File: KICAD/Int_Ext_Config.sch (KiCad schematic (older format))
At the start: 7 parts, among them J3 Conn_01x17_Male

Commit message: removed legacy symbols
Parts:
- removed J3: Conn_01x17_Male, symbol Connector:Conn_01x17_Male
- removed JP1: CC-CV, symbol sesame-fonctionnel-rescue:Jumper-device
- removed JP2, JP3: Jumper, symbol sesame-fonctionnel-rescue:Jumper-device
- removed R5, R6, R7: R, symbol sesame-fonctionnel-rescue:R-device
- added J?: Conn_01x17_Male, symbol Connector:Conn_01x17_Male
- added JP? (x3): Jumper, symbol Device:Jumper
- added R? (x3): R, symbol Device:R
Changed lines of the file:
@@
 $Descr A4 11693 8268
 encoding utf-8
-Sheet 10 15
+Sheet 9 15
 Title ""
 Date ""
@@
 Text GLabel 5300 5450 2    50   Output ~ 0
 Ex_CC_CV_Mode
-Text GLabel 5750 3200 2    50   Output ~ 0
+Text GLabel 6100 3200 2    50   Output ~ 0
 Mode
-$Comp
-L sesame-fonctionnel-rescue:Jumper-device JP3
-U 1 1 6188609D
-P 5000 3200
-AR Path="/6188609D" Ref="JP3"  Part="1"
-AR Path="/618748E2/6188609D" Ref="JP3"  Part="1"
-F 0 "JP3" H 5000 3464 50  0000 C CNN
-F 1 "Jumper" H 5000 3373 50  0000 C CNN
-F 2 "" H 5000 3200 50  0001 C CNN
-F 3 "~" H 5000 3200 50  0001 C CNN
-	1    5000 3200
-	1    0    0    -1
-$EndComp
 Wire Wire Line
 	4700 3200 4650 3200
@@
 Wire Wire Line
 	5650 3950 5650 4150
-Wire Wire Line
-	5650 4150 5000 4150
-Wire Wire Line
-	5450 4050 5000 4050
 Wire Wire Line
 	5450 3950 5450 4050
@@
 Wire Wire Line
 	5300 4950 5000 4950
-Wire Wire Line
-	5300 4250 5000 4250
-Wire Wire Line
-	5000 4350 5300 4350
-Wire Wire Line
-	5300 4450 5000 4450
-Wire Wire Line
-	5000 4550 5300 4550
-Connection ~ 5650 3200
-Wire Wire Line
-	5650 3200 5750 3200
-Wire Wire Line
-	5300 3200 5650 3200
 Connection ~ 4650 3200
 Wire Wire Line
-	5500 1900 5500 1800
-Connection ~ 5500 1900
-Wire Wire Line
-	5650 1900 5500 1900
-Wire Wire Line
-	5650 2300 5650 3200
-Connection ~ 5500 2800
-Wire Wire Line
-	5500 2800 5750 2800
-Connection ~ 5350 2400
-Wire Wire Line
-	5750 2400 5350 2400
-Wire Wire Line
-	5500 2300 5500 2800
+	5600 1900 5600 1800
 Connection ~ 4650 2800
 Wire Wire Line
@@
 Wire Wire Line
 	4700 2800 4650 2800
-$Comp
-L sesame-fonctionnel-rescue:Jumper-device JP1
-U 1 1 618860D7
-P 5000 2400
-AR Path="/618860D7" Ref="JP1"  Part="1"
-AR Path="/618748E2/618860D7" Ref="JP1"  Part="1"
-F 0 "JP1" H 5000 2664 50  0000 C CNN
-F 1 "CC-CV" H 5000 2573 50  0000 C CNN
-F 2 "" H 5000 2400 50  0001 C CNN
-F 3 "~" H 5000 2400 50  0001 C CNN
-	1    5000 2400
-	1    0    0    -1
-$EndComp
-$Comp
-L sesame-fonctionnel-rescue:Jumper-device JP2
-U 1 1 618860DD
-P 5000 2800
-AR Path="/618860DD" Ref="JP2"  Part="1"
-AR Path="/618748E2/618860DD" Ref="JP2"  Part="1"
-F 0 "JP2" H 5000 3064 50  0000 C CNN
-F 1 "Jumper" H 5000 2973 50  0000 C CNN
-F 2 "" H 5000 2800 50  0001 C CNN
-F 3 "~" H 5000 2800 50  0001 C CNN
-	1    5000 2800
-	1    0    0    -1
-$EndComp
-Text GLabel 5750 2400 2    50   Output ~ 0
+Text GLabel 6100 2400 2    50   Output ~ 0
 CC_CV_Mode
-$Comp
-L sesame-fonctionnel-rescue:R-device R5
-U 1 1 618860E4
-P 5350 2150
-AR Path="/618860E4" Ref="R5"  Part="1"
-AR Path="/618748E2/618860E4" Ref="R5"  Part="1"
-F 0 "R5" H 5250 2300 50  0000 L CNN
-F 1 "R" H 5250 2200 50  0000 L CNN
-F 2 "" V 5280 2150 50  0001 C CNN
-F 3 "~" H 5350 2150 50  0001 C CNN
-	1    5350 2150
-	1    0    0    -1
-$EndComp
 $Comp
 L power:VCC #PWR0112
 U 1 1 618860EA
-P 5500 1800
-F 0 "#PWR0112" H 5500 1650 50  0001 C CNN
-F 1 "VCC" H 5515 1973 50  0000 C CNN
-F 2 "" H 5500 1800 50  0001 C CNN
-F 3 "" H 5500 1800 50  0001 C CNN
-	1    5500 1800
+P 5600 1800
+F 0 "#PWR0112" H 5600 1650 50  0001 C CNN
+F 1 "VCC" H 5615 1973 50  0000 C CNN
+F 2 "" H 5600 1800 50  0001 C CNN
+F 3 "" H 5600 1800 50  0001 C CNN
+	1    5600 1800
 	1    0    0    -1
 $EndComp
 Wire Wire Line
 	5350 2400 5300 2400
-Wire Wire Line
-	5350 2300 5350 2400
-Text GLabel 5750 2800 2    50   Output ~ 0
+Text GLabel 6100 2800 2    50   Output ~ 0
 Dir
-$Comp
-L sesame-fonctionnel-rescue:R-device R6
-U 1 1 618860F3
-P 5500 2150
-AR Path="/618860F3" Ref="R6"  Part="1"
-AR Path="/618748E2/618860F3" Ref="R6"  Part="1"
-F 0 "R6" H 5400 2300 50  0000 L CNN
-F 1 "R" H 5400 2200 50  0000 L CNN
-F 2 "" V 5430 2150 50  0001 C CNN
-F 3 "~" H 5500 2150 50  0001 C CNN
-	1    5500 2150
-	1    0    0    -1
-$EndComp
-Wire Wire Line
-	5500 2800 5300 2800
-Wire Wire Line
-	5500 2000 5500 1900
-Wire Wire Line
-	5500 1900 5350 1900
 Wire Wire Line
 	5350 1900 5350 2000
-$Comp
-L sesame-fonctionnel-rescue:R-device R7
-U 1 1 618860FD
-P 5650 2150
-AR Path="/618860FD" Ref="R7"  Part="1"
-AR Path="/618748E2/618860FD" Ref="R7"  Part="1"
-F 0 "R7" H 5550 2300 50  0000 L CNN
-F 1 "R" H 5550 2200 50  0000 L CNN
-F 2 "" V 5580 2150 50  0001 C CNN
-F 3 "~" H 5650 2150 50  0001 C CNN
-	1    5650 2150
-	1    0    0    -1
-$EndComp
-Wire Wire Line
-	5650 2000 5650 1900
 Text GLabel 5300 4750 2    50   Output ~ 0
 Ex_PWM
@@
 Text GLabel 5300 4650 2    50   Output ~ 0
 Ex_Consign
-$Comp
-L Connector:Conn_01x17_Male J3
-U 1 1 61886109
-P 4800 4750
-F 0 "J3" H 4908 5731 50  0000 C CNN
-F 1 "Conn_01x17_Male" H 4908 5640 50  0000 C CNN
-F 2 "" H 4800 4750 50  0001 C CNN
-F 3 "~" H 4800 4750 50  0001 C CNN
-	1    4800 4750
-	1    0    0    -1
-$EndComp
-Wire Wire Line
-	5300 4650 5000 4650
 Text HLabel 5300 4250 2    50   Input ~ 0
 Current_Sens_L
@@
 Text HLabel 5300 4550 2    50   Input ~ 0
 Voltage_Sens_R
+$Comp
+L Device:Jumper JP?
+U 1 1 61093A28
+P 5000 2800
+F 0 "JP?" H 5000 3064 50  0000 C CNN
+F 1 "Jumper" H 5000 2973 50  0000 C CNN
+F 2 "" H 5000 2800 50  0001 C CNN
+F 3 "~" H 5000 2800 50  0001 C CNN
+	1    5000 2800
+	1    0    0    -1
+$EndComp
+$Comp
+L Device:Jumper JP?
+U 1 1 61098F8F
+P 5000 2400
+F 0 "JP?" H 5000 2664 50  0000 C CNN
+F 1 "Jumper" H 5000 2573 50  0000 C CNN
+F 2 "" H 5000 2400 50  0001 C CNN
+F 3 "~" H 5000 2400 50  0001 C CNN
+	1    5000 2400
+	1    0    0    -1
+$EndComp
+$Comp
+L Device:Jumper JP?
+U 1 1 6109AD40
+P 5000 3200
+F 0 "JP?" H 5000 3464 50  0000 C CNN
+F 1 "Jumper" H 5000 3373 50  0000 C CNN
+F 2 "" H 5000 3200 50  0001 C CNN
+F 3 "~" H 5000 3200 50  0001 C CNN
+	1    5000 3200
+	1    0    0    -1
+$EndComp
+$Comp
+L Device:R R?
+U 1 1 6109B89A
+P 5350 2150
+F 0 "R?" H 5420 2196 50  0000 L CNN
+F 1 "R" H 5420 2105 50  0000 L CNN
+F 2 "" V 5280 2150 50  0001 C CNN
+F 3 "~" H 5350 2150 50  0001 C CNN
+	1    5350 2150
+	1    0    0    -1
+$EndComp
+$Comp
+L Device:R R?
+U 1 1 6109EABF
+P 5600 2150
+F 0 "R?" H 5670 2196 50  0000 L CNN
+F 1 "R" H 5670 2105 50  0000 L CNN
+F 2 "" V 5530 2150 50  0001 C CNN
+F 3 "~" H 5600 2150 50  0001 C CNN
+	1    5600 2150
+	1    0    0    -1
+$EndComp
+$Comp
+L Device:R R?
+U 1 1 6109F746
+P 5850 2150
+F 0 "R?" H 5920 2196 50  0000 L CNN
+F 1 "R" H 5920 2105 50  0000 L CNN
+F 2 "" V 5780 2150 50  0001 C CNN
+F 3 "~" H 5850 2150 50  0001 C CNN
+	1    5850 2150
+	1    0    0    -1
+$EndComp
+Connection ~ 5600 1900
+Wire Wire Line
+	5350 1900 5600 1900
+Wire Wire Line
+	5600 2000 5600 1900
+Wire Wire Line
+	5850 1900 5850 2000
+Wire Wire Line
+	5600 1900 5850 1900
+Wire Wire Line
+	5300 3200 5850 3200
+Wire Wire Line
+	5300 2800 5600 2800
+Wire Wire Line
+	5350 2300 5350 2400
+Connection ~ 5600 2800
+Wire Wire Line
+	5600 2800 6100 2800
+Wire Wire Line
+	5600 2300 5600 2800
+Wire Wire Line
+	5850 2300 5850 3200
+Connection ~ 5850 3200
+Wire Wire Line
+	5850 3200 6100 3200
+Wire Wire Line
+	5350 2400 6100 2400
+Connection ~ 5350 2400
+$Comp
+L Connector:Conn_01x17_Male J?
+U 1 1 610AA20B
+P 4800 4750
+F 0 "J?" H 4908 5731 50  0000 C CNN
+F 1 "Conn_01x17_Male" H 4908 5640 50  0000 C CNN
+F 2 "" H 4800 4750 50  0001 C CNN
+F 3 "~" H 4800 4750 50  0001 C CNN
+	1    4800 4750
+	1    0    0    -1
+$EndComp
+Wire Wire Line
+	5000 4650 5300 4650
+Wire Wire Line
+	5300 4550 5000 4550
+Wire Wire Line
+	5000 4450 5300 4450
+Wire Wire Line
+	5300 4350 5000 4350
+Wire Wire Line
+	5000 4250 5300 4250
+Wire Wire Line
+	5650 4150 5000 4150
+Wire Wire Line
+	5000 4050 5450 4050
 $EndSCHEMATC

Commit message: a ton of new stuff. V0.8
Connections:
- net labels added: +6V, +7V
- net labels removed: +2V5, VCC
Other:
- note added: "A voir au dernier moment"
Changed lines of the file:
@@
 $Descr A4 11693 8268
 encoding utf-8
-Sheet 8 15
+Sheet 8 16
 Title ""
 Date ""
@@
 Wire Wire Line
 	5450 3950 5450 4050
-$Comp
-L power:VCC #PWR0110
-U 1 1 618860AB
-P 5450 3950
-F 0 "#PWR0110" H 5450 3800 50  0001 C CNN
-F 1 "VCC" H 5465 4123 50  0000 C CNN
-F 2 "" H 5450 3950 50  0001 C CNN
-F 3 "" H 5450 3950 50  0001 C CNN
-	1    5450 3950
-	1    0    0    -1
-$EndComp
-$Comp
-L power:+2V5 #PWR0111
-U 1 1 618860B1
-P 5650 3950
-F 0 "#PWR0111" H 5650 3800 50  0001 C CNN
-F 1 "+2V5" H 5665 4123 50  0000 C CNN
-F 2 "" H 5650 3950 50  0001 C CNN
-F 3 "" H 5650 3950 50  0001 C CNN
-	1    5650 3950
-	1    0    0    -1
-$EndComp
 Text GLabel 5300 5150 2    50   Output ~ 0
 Ex_Rearm
@@
 Text GLabel 6100 2400 2    50   Output ~ 0
 CC_CV_Mode
-$Comp
-L power:VCC #PWR0112
-U 1 1 618860EA
-P 5600 1800
-F 0 "#PWR0112" H 5600 1650 50  0001 C CNN
-F 1 "VCC" H 5615 1973 50  0000 C CNN
-F 2 "" H 5600 1800 50  0001 C CNN
-F 3 "" H 5600 1800 50  0001 C CNN
-	1    5600 1800
-	1    0    0    -1
-$EndComp
 Wire Wire Line
 	5350 2400 5300 2400
@@
 Wire Wire Line
 	5000 4050 5450 4050
+Text Notes 4550 950  0    100  ~ 20
+A voir au dernier moment
+$Comp
+L Sesame:+7V #PWR0128
+U 1 1 61485513
+P 5600 1800
+F 0 "#PWR0128" H 5600 1650 50  0001 C CNN
+F 1 "+7V" H 5615 1973 50  0000 C CNN
+F 2 "" H 5600 1800 50  0001 C CNN
+F 3 "" H 5600 1800 50  0001 C CNN
+	1    5600 1800
+	1    0    0    -1
+$EndComp
+$Comp
+L Sesame:+7V #PWR0129
+U 1 1 61487244
+P 5450 3950
+F 0 "#PWR0129" H 5450 3800 50  0001 C CNN
+F 1 "+7V" H 5465 4123 50  0000 C CNN
+F 2 "" H 5450 3950 50  0001 C CNN
+F 3 "" H 5450 3950 50  0001 C CNN
+	1    5450 3950
+	1    0    0    -1
+$EndComp
+$Comp
+L power:+6V #PWR0130
+U 1 1 61487948
+P 5650 3950
+F 0 "#PWR0130" H 5650 3800 50  0001 C CNN
+F 1 "+6V" H 5665 4123 50  0000 C CNN
+F 2 "" H 5650 3950 50  0001 C CNN
+F 3 "" H 5650 3950 50  0001 C CNN
+	1    5650 3950
+	1    0    0    -1
+$EndComp
 $EndSCHEMATC

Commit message: minor cleanup
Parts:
- removed J?: Conn_01x17_Male, symbol Connector:Conn_01x17_Male
- removed JP? (x3): Jumper, symbol Device:Jumper
- removed R? (x3): R, symbol Device:R
- added J?: Conn_02x16_Odd_Even, symbol Connector_Generic:Conn_02x16_Odd_Even
- added JP? (x5): Jumper_NC_Dual, symbol Device:Jumper_NC_Dual
- added R? (x3): R, symbol Device:R
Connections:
- net CC_CV_Mode: now also J?.32 (Pin_32), R?.2
- net Current_Sens_L: now also J?.8 (Pin_8)
- net Current_Sens_R: now also J?.12 (Pin_12)
- net Dir: now also J?.30 (Pin_30), R?.2
- net GND: now also J?.1 (Pin_1), J?.11 (Pin_11), J?.13 (Pin_13), J?.15 (Pin_15), J?.17 (Pin_17), J?.19 (Pin_19), J?.21 (Pin_21), J?.23 (Pin_23), J?.25 (Pin_25), J?.27 (Pin_27), J?.29 (Pin_29), J?.3 (Pin_3), J?.31 (Pin_31), J?.5 (Pin_5), J?.7 (Pin_7), J?.9 (Pin_9), JP?.1, JP?.1, JP?.1
- net Mode: now also J?.28 (Pin_28), R?.2
- net Voltage_Sens_L: now also J?.10 (Pin_10)
- net Voltage_Sens_R: now also J?.14 (Pin_14)
- new net: JP?.2, R?.1 (x3)
- new net Ext_Current_Tresh: J?.22 (Pin_22)
- new net Ext_PWM: J?.18 (Pin_18), JP?.3
- new net Ext_Rearm: J?.26 (Pin_26)
- new net Ext_Setpoint: J?.16 (Pin_16)
- new net Ext_Voltage_Tresh: J?.24 (Pin_24)
- new net INT_PWM: JP?.1
- new net PWM: JP?.2
- new net VCC: J?.2 (Pin_2), J?.4 (Pin_4), JP?.3, JP?.3, JP?.3
- new net VREF: J?.6 (Pin_6)
- new net ~Ext_PWM: J?.20 (Pin_20), JP?.3
- new net ~INT_PWM: JP?.1
- new net ~PWM: JP?.2
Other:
- note removed: "A voir au dernier moment"

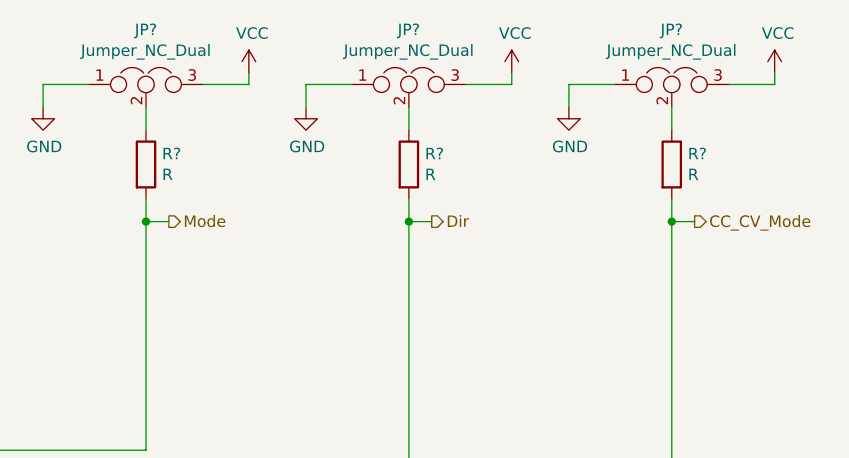
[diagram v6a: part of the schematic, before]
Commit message: drivers draft + clean and minors changes
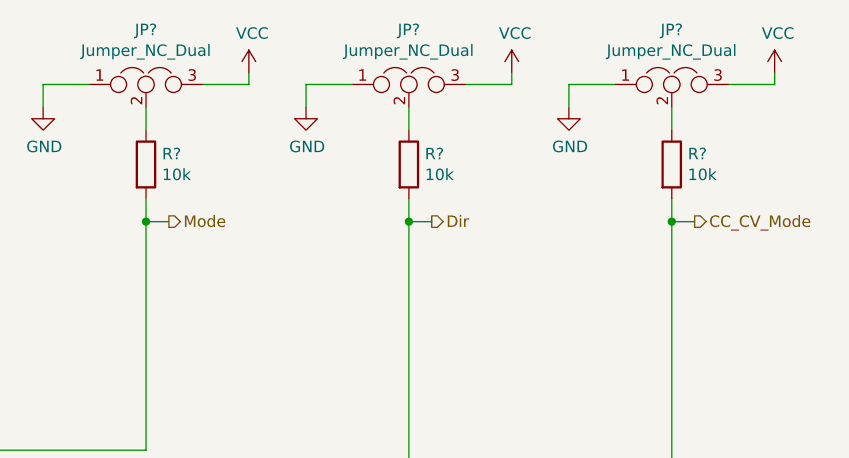
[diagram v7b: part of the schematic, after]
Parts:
- R? (x3): value R -> 10k
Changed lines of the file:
@@
 $Descr A4 11693 8268
 encoding utf-8
-Sheet 2 16
+Sheet 15 16
 Title ""
 Date ""
@@
 P 8150 4000
 F 0 "R?" H 8220 4046 50  0000 L CNN
-F 1 "R" H 8220 3955 50  0000 L CNN
+F 1 "10k" H 8220 3955 50  0000 L CNN
 F 2 "" V 8080 4000 50  0001 C CNN
 F 3 "~" H 8150 4000 50  0001 C CNN
@@
 P 9300 4000
 F 0 "R?" H 9370 4046 50  0000 L CNN
-F 1 "R" H 9370 3955 50  0000 L CNN
+F 1 "10k" H 9370 3955 50  0000 L CNN
 F 2 "" V 9230 4000 50  0001 C CNN
 F 3 "~" H 9300 4000 50  0001 C CNN
@@
 P 10450 4000
 F 0 "R?" H 10520 4046 50  0000 L CNN
-F 1 "R" H 10520 3955 50  0000 L CNN
+F 1 "10k" H 10520 3955 50  0000 L CNN
 F 2 "" V 10380 4000 50  0001 C CNN
 F 3 "~" H 10450 4000 50  0001 C CNN
